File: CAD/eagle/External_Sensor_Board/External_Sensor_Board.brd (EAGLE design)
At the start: 50.8 x 33 mm, 12 parts, among them J1 SFW15R_FFC, U1 MAX31725MTA+, U2 HSCMNNN1.6BAAA3

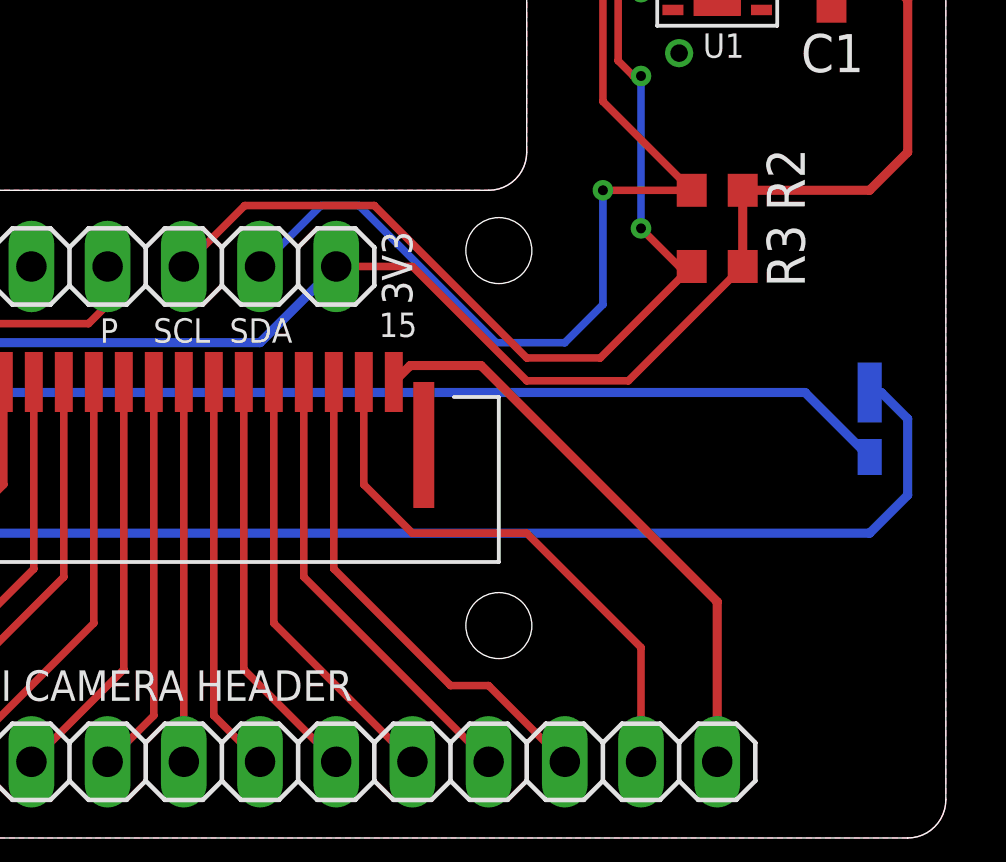
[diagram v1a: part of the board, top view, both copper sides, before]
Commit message: Added I2C buffer to external sensor board.
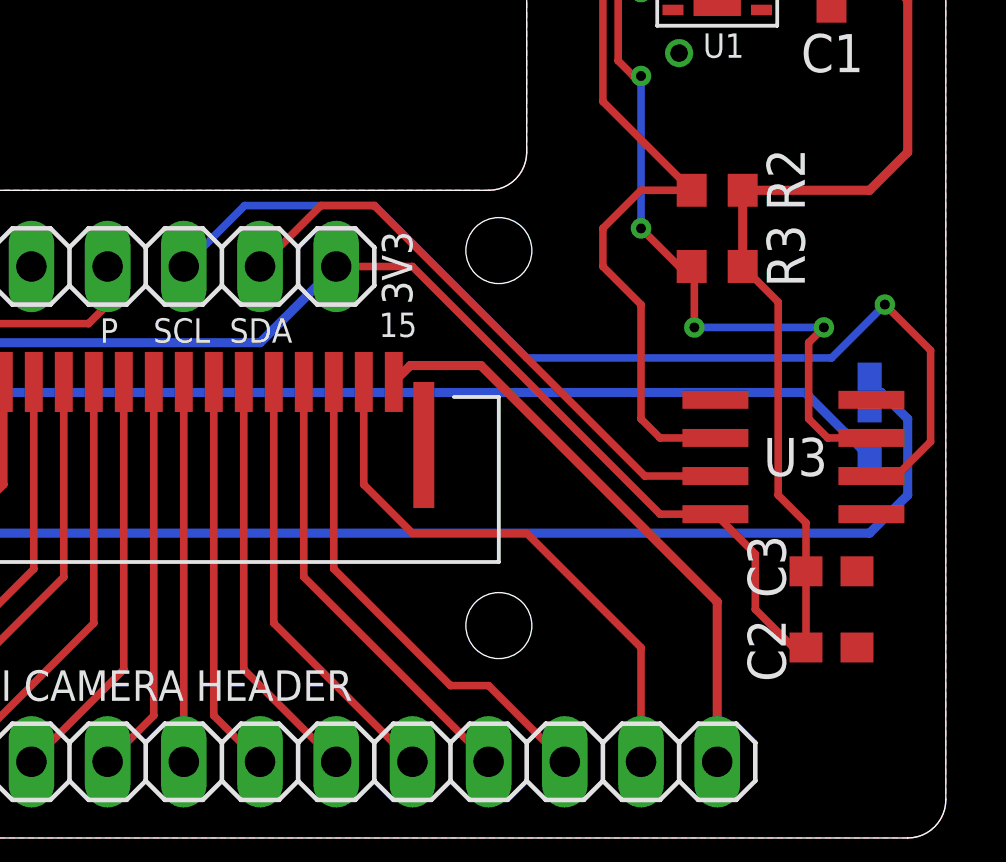
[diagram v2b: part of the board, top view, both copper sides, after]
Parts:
- added C2: 1uF, resistor:C0603
- added C3: 100nF, resistor:C0603
- added U3: P82B715, CM_IC:SO8
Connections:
- new net SCL_BUFF: JP1.3, U3.2
- new net SDA_BUFF: JP1.2, U3.7
- net +3V3: now also C2.1, C3.1, U3.8
- net GND: now also C2.2, C3.2, U3.4
- net SCL: now also U3.3; no longer JP1.3
- net SDA: now also U3.6; no longer JP1.2
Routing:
- net SCL_BUFF: track 0.00 -> 34.7 mm, vias 0 -> 1
- net SDA_BUFF: track 0.00 -> 19.8 mm
- net +3V3: track 71.2 -> 90.0 mm
- net SCL: track 34.0 -> 24.9 mm, vias 2 -> 4
- net SDA: track 32.8 -> 24.4 mm, vias 1 -> 0
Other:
- board text removed: "OPTIONAL"
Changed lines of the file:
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@@
 <layer number="48" name="Document" color="7" fill="1" visible="yes" active="yes"/>
 <layer number="49" name="Reference" color="7" fill="1" visible="yes" active="yes"/>
+<layer number="50" name="dxf" color="7" fill="1" visible="no" active="no"/>
 <layer number="51" name="tDocu" color="7" fill="1" visible="yes" active="yes"/>
 <layer number="52" name="bDocu" color="7" fill="1" visible="yes" active="yes"/>
@@
 <layer number="98" name="Guide" color="6" fill="1" visible="no" active="no"/>
 <layer number="99" name="SpiceOrder" color="5" fill="1" visible="no" active="no"/>
+<layer number="100" name="Muster" color="7" fill="1" visible="no" active="no"/>
+<layer number="101" name="Patch_Top" color="12" fill="4" visible="yes" active="yes"/>
+<layer number="116" name="Patch_BOT" color="9" fill="4" visible="yes" active="yes"/>
+<layer number="200" name="200bmp" color="1" fill="10" visible="no" active="no"/>
+<layer number="250" name="Descript" color="3" fill="1" visible="yes" active="yes"/>
+<layer number="251" name="SMDround" color="12" fill="11" visible="no" active="no"/>
 </layers>
 <board>
@@
 <text x="24.384" y="16.51" size="0.8128" layer="21">SCL</text>
 <text x="26.924" y="16.51" size="0.8128" layer="21">SDA</text>
-<text x="49.53" y="17.78" size="0.8128" layer="51" rot="R180">I2C PULLUPS</text>
-<text x="47.244" y="16.764" size="0.8128" layer="51" rot="R180">OPTIONAL</text>
+<text x="46.228" y="24.384" size="0.8128" layer="51" rot="R270">I2C PULLUPS</text>
 <dimension x1="0" y1="31.75" x2="50.8" y2="27.94" x3="25.4" y3="39.37" textsize="0.8128" layer="49" dtype="horizontal" unit="inch"/>
 <dimension x1="38.1" y1="31.75" x2="37.201975" y2="32.648025" x3="31.686540625" y3="38.163459375" textsize="0.8128" layer="49" dtype="radius" unit="inch"/>
@@
 <attribute name="NAME" x="2.794" y="21.844" size="0.8128" layer="25" rot="R180"/>
 </element>
+<element name="U3" library="CM_IC" package="SO8" value="P82B715" x="45.72" y="12.7" smashed="yes" rot="R90">
+<attribute name="NAME" x="46.863" y="13.335" size="1.27" layer="25" rot="R180"/>
+</element>
+<element name="C2" library="resistor" package="C0603" value="1uF" x="46.99" y="6.35" smashed="yes">
+<attribute name="NAME" x="45.466" y="5.207" size="1.27" layer="25" rot="R90"/>
+</element>
+<element name="C3" library="resistor" package="C0603" value="100nF" x="46.99" y="8.89" smashed="yes">
+<attribute name="NAME" x="45.466" y="8.001" size="1.27" layer="25" rot="R90"/>
+</element>
 </elements>
 <signals>
@@
 <wire x1="44.655" y1="30.685" x2="45.1925" y2="31.2225" width="0.3048" layer="1"/>
 <wire x1="30.48" y1="19.05" x2="33.02" y2="19.05" width="0.254" layer="1"/>
-<wire x1="33.02" y1="19.05" x2="36.83" y2="15.24" width="0.254" layer="1"/>
-<wire x1="36.83" y1="15.24" x2="40.22" y2="15.24" width="0.254" layer="1"/>
-<wire x1="40.22" y1="15.24" x2="44.03" y2="19.05" width="0.254" layer="1"/>
+<contactref element="C2" pad="1"/>
+<contactref element="C3" pad="1"/>
+<contactref element="U3" pad="8"/>
+<wire x1="33.02" y1="19.05" x2="41.275" y2="10.795" width="0.254" layer="1"/>
+<wire x1="41.275" y1="10.795" x2="43.12" y2="10.795" width="0.254" layer="1"/>
+<wire x1="45.212" y1="11.43" x2="45.212" y2="17.868" width="0.254" layer="1"/>
+<wire x1="45.212" y1="17.868" x2="44.03" y2="19.05" width="0.254" layer="1"/>
+<wire x1="45.212" y1="11.43" x2="46.14" y2="10.502" width="0.254" layer="1"/>
+<wire x1="46.14" y1="10.502" x2="46.14" y2="8.89" width="0.254" layer="1"/>
+<wire x1="46.14" y1="8.89" x2="46.14" y2="6.35" width="0.254" layer="1"/>
+<wire x1="43.12" y1="10.795" x2="44.45" y2="9.465" width="0.254" layer="1"/>
+<wire x1="44.45" y1="9.465" x2="44.45" y2="7.62" width="0.254" layer="1"/>
+<wire x1="44.45" y1="7.62" x2="45.72" y2="6.35" width="0.254" layer="1"/>
+<wire x1="45.72" y1="6.35" x2="46.14" y2="6.35" width="0.254" layer="1"/>
 </signal>
 <signal name="GND">
@@
 </polygon>
 <via x="41.91" y="26.162" extent="1-16" drill="0.5842"/>
+<contactref element="U3" pad="4"/>
+<contactref element="C3" pad="2"/>
+<contactref element="C2" pad="2"/>
 </signal>
 <signal name="SDA">
 <contactref element="U1" pad="1"/>
 <contactref element="R2" pad="2"/>
-<contactref element="JP1" pad="2"/>
-<via x="39.37" y="21.59" extent="1-16" drill="0.3302"/>
-<wire x1="39.37" y1="21.59" x2="42.33" y2="21.59" width="0.254" layer="1"/>
 <wire x1="42.33" y1="21.59" x2="39.37" y2="24.55" width="0.254" layer="1"/>
 <wire x1="39.37" y1="24.55" x2="39.37" y2="29.21" width="0.254" layer="1"/>
 <wire x1="39.37" y1="29.21" x2="39.71" y2="29.55" width="0.254" layer="1"/>
 <wire x1="39.71" y1="29.55" x2="41.705" y2="29.55" width="0.254" layer="1"/>
-<wire x1="27.94" y1="19.05" x2="29.972" y2="21.082" width="0.254" layer="16"/>
-<wire x1="29.972" y1="21.082" x2="31.242" y2="21.082" width="0.254" layer="16"/>
-<wire x1="31.242" y1="21.082" x2="35.814" y2="16.51" width="0.254" layer="16"/>
-<wire x1="35.814" y1="16.51" x2="38.1" y2="16.51" width="0.254" layer="16"/>
-<wire x1="38.1" y1="16.51" x2="39.37" y2="17.78" width="0.254" layer="16"/>
-<wire x1="39.37" y1="17.78" x2="39.37" y2="21.59" width="0.254" layer="16"/>
+<contactref element="U3" pad="6"/>
+<wire x1="43.12" y1="13.335" x2="41.275" y2="13.335" width="0.254" layer="1"/>
+<wire x1="41.275" y1="13.335" x2="40.64" y2="13.97" width="0.254" layer="1"/>
+<wire x1="40.64" y1="13.97" x2="40.64" y2="17.78" width="0.254" layer="1"/>
+<wire x1="40.64" y1="17.78" x2="39.37" y2="19.05" width="0.254" layer="1"/>
+<wire x1="39.37" y1="19.05" x2="39.37" y2="20.32" width="0.254" layer="1"/>
+<wire x1="39.37" y1="20.32" x2="40.64" y2="21.59" width="0.254" layer="1"/>
+<wire x1="40.64" y1="21.59" x2="42.33" y2="21.59" width="0.254" layer="1"/>
 </signal>
 <signal name="SCL">
 <contactref element="U1" pad="2"/>
 <contactref element="R3" pad="2"/>
-<contactref element="JP1" pad="3"/>
 <wire x1="42.33" y1="19.05" x2="41.91" y2="19.05" width="0.254" layer="1"/>
 <via x="40.64" y="20.32" extent="1-16" drill="0.3302"/>
@@
 <wire x1="41.649" y1="28.956" x2="41.705" y2="28.9" width="0.254" layer="1"/>
 <wire x1="40.64" y1="20.32" x2="41.91" y2="19.05" width="0.254" layer="1"/>
-<wire x1="25.4" y1="19.05" x2="27.432" y2="21.082" width="0.254" layer="1"/>
-<wire x1="27.432" y1="21.082" x2="31.75" y2="21.082" width="0.254" layer="1"/>
-<wire x1="31.75" y1="21.082" x2="36.83" y2="16.002" width="0.254" layer="1"/>
-<wire x1="36.83" y1="16.002" x2="39.282" y2="16.002" width="0.254" layer="1"/>
-<wire x1="39.282" y1="16.002" x2="42.33" y2="19.05" width="0.254" layer="1"/>
+<contactref element="U3" pad="3"/>
+<wire x1="48.32" y1="13.335" x2="46.863" y2="13.335" width="0.254" layer="1"/>
+<wire x1="46.863" y1="13.335" x2="46.228" y2="13.97" width="0.254" layer="1"/>
+<wire x1="46.228" y1="13.97" x2="46.228" y2="16.51" width="0.254" layer="1"/>
+<wire x1="46.228" y1="16.51" x2="46.736" y2="17.018" width="0.254" layer="1"/>
+<via x="46.736" y="17.018" extent="1-16" drill="0.3302"/>
+<wire x1="46.736" y1="17.018" x2="42.418" y2="17.018" width="0.254" layer="16"/>
+<via x="42.418" y="17.018" extent="1-16" drill="0.3302"/>
+<wire x1="42.418" y1="17.018" x2="42.418" y2="18.962" width="0.254" layer="1"/>
+<wire x1="42.418" y1="18.962" x2="42.33" y2="19.05" width="0.254" layer="1"/>
 </signal>
 <signal name="N$1">
@@
 <wire x1="27.4" y1="5.62" x2="27.4" y2="15.2" width="0.254" layer="1"/>
 </signal>
+<signal name="SDA_BUFF">
+<contactref element="U3" pad="7"/>
+<contactref element="JP1" pad="2"/>
+<wire x1="27.94" y1="19.05" x2="29.972" y2="21.082" width="0.254" layer="1"/>
+<wire x1="29.972" y1="21.082" x2="31.75" y2="21.082" width="0.254" layer="1"/>
+<wire x1="31.75" y1="21.082" x2="40.767" y2="12.065" width="0.254" layer="1"/>
+<wire x1="40.767" y1="12.065" x2="43.12" y2="12.065" width="0.254" layer="1"/>
+</signal>
+<signal name="SCL_BUFF">
+<contactref element="U3" pad="2"/>
+<contactref element="JP1" pad="3"/>
+<wire x1="25.4" y1="19.05" x2="27.432" y2="21.082" width="0.254" layer="16"/>
+<wire x1="27.432" y1="21.082" x2="31.75" y2="21.082" width="0.254" layer="16"/>
+<wire x1="31.75" y1="21.082" x2="36.83" y2="16.002" width="0.254" layer="16"/>
+<wire x1="36.83" y1="16.002" x2="46.99" y2="16.002" width="0.254" layer="16"/>
+<wire x1="46.99" y1="16.002" x2="48.768" y2="17.78" width="0.254" layer="16"/>
+<via x="48.768" y="17.78" extent="1-16" drill="0.3302"/>
+<wire x1="48.768" y1="17.78" x2="50.292" y2="16.256" width="0.254" layer="1"/>
+<wire x1="50.292" y1="16.256" x2="50.292" y2="13.208" width="0.254" layer="1"/>
+<wire x1="50.292" y1="13.208" x2="49.149" y2="12.065" width="0.254" layer="1"/>
+<wire x1="49.149" y1="12.065" x2="48.32" y2="12.065" width="0.254" layer="1"/>
+</signal>
 </signals>

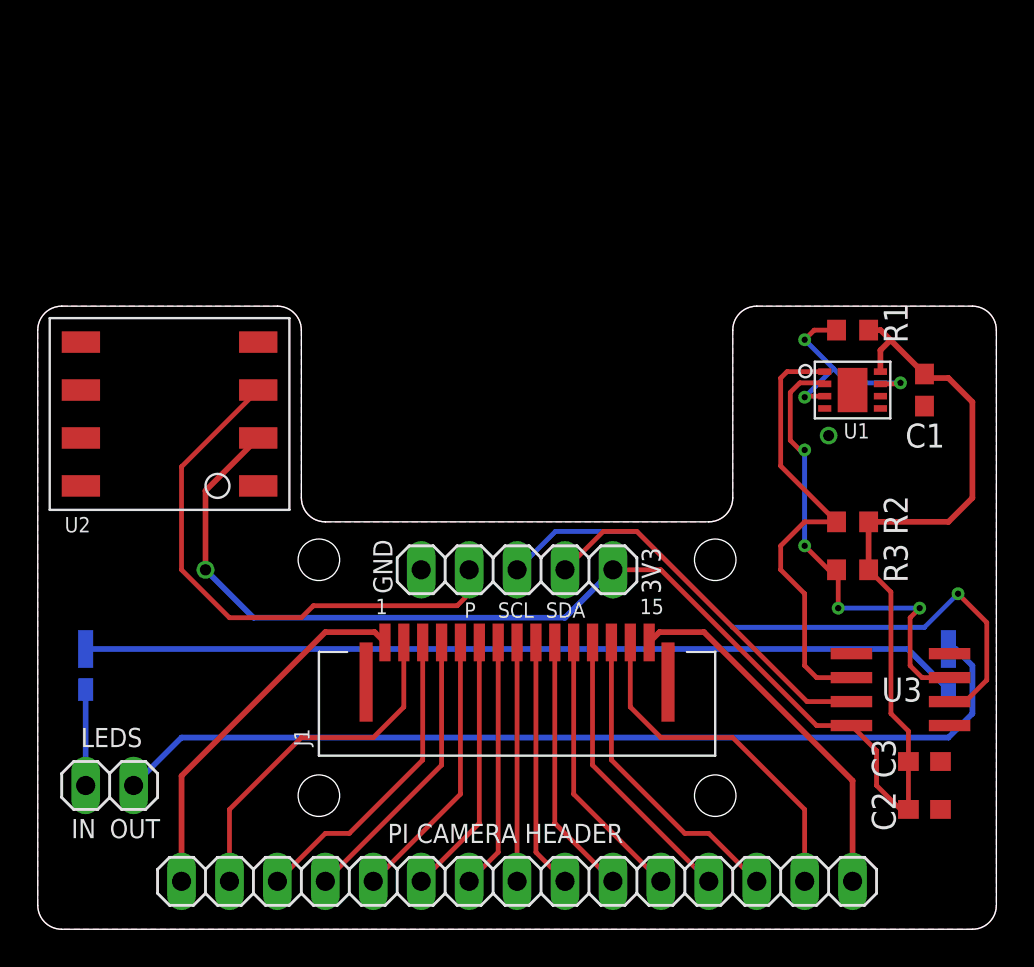
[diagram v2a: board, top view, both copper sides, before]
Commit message: Altered external sensor board to use J30J-25 connector instead of headers. Board is final aside from logos.
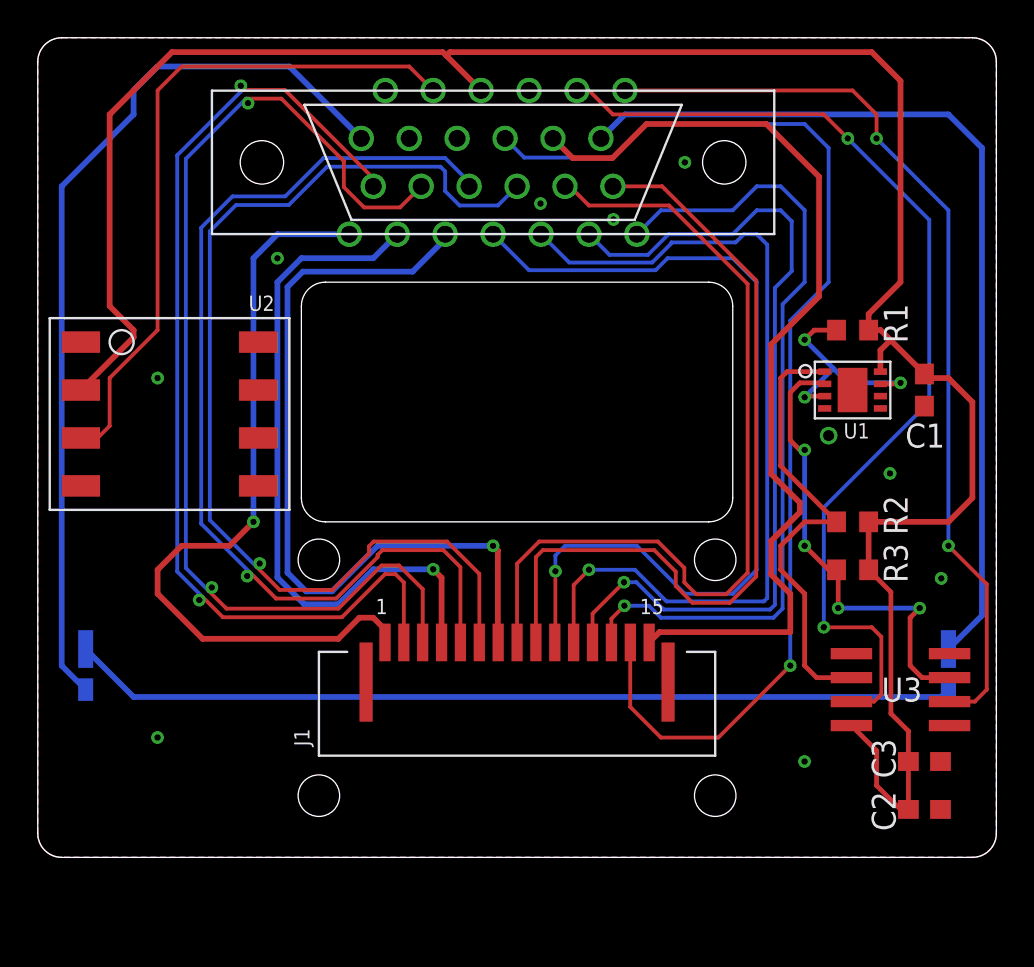
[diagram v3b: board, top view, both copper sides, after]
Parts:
- removed JP1: (no value), pinhead:1X05
- removed JP2: (no value), pinhead:1X15
- removed JP3: (no value), pinhead:1X02
- added J2: J30J-25, CM_J30J:ZKN-25
- turned U2 to 270 degrees
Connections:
- removed net CAM_CN: J1.8, JP2.8
- removed net CAM_CP: J1.9, JP2.9
- removed net CAM_DN0: J1.2, JP2.2
- removed net CAM_DN1: J1.5, JP2.5
- removed net CAM_DP0: J1.3, JP2.3
- removed net CAM_DP1: J1.6, JP2.6
- new net CAM_C_N: J1.8, J2.10
- new net CAM_C_P: J1.9, J2.12
- new net CAM_D0_N: J1.2, J2.2
- new net CAM_D0_P: J1.3, J2.4
- new net CAM_D1_N: J1.5, J2.6
- new net CAM_D1_P: J1.6, J2.8
- net +3V3: now also J2.19; no longer JP1.1
- net CAM_3V3: now also J2.22; no longer JP2.15
- net CAM_GND1: now also J2.1; no longer JP2.1
- net CAM_GND2: now also J2.3; no longer JP2.4
- net CAM_GND3: now also J2.5; no longer JP2.7
- net CAM_GND4: now also J2.7; no longer JP2.10
- net CAM_GPIO0: now also J2.9; no longer JP2.11
- net CAM_GPIO1: now also J2.11; no longer JP2.12
- net CAM_SCL: now also J2.13; no longer JP2.13
- net CAM_SDA: now also J2.20; no longer JP2.14
- net GND: now also J2.15; no longer JP1.5
- net LED_IN: now also J2.14; no longer JP3.1
- net LED_OUT: now also J2.24; no longer JP3.2
- net POUT: now also J2.17; no longer JP1.4
- net SCL_BUFF: now also J2.25; no longer JP1.3
- net SDA_BUFF: now also J2.23; no longer JP1.2
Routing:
- net CAM_D0_P: track 0.00 -> 57.9 mm, vias 0 -> 2
- net CAM_D1_P: track 0.00 -> 56.8 mm, vias 0 -> 1
- net CAM_D0_N: track 0.00 -> 54.5 mm, vias 0 -> 2
- net CAM_D1_N: track 0.00 -> 53.5 mm, vias 0 -> 1
- net CAM_C_N: track 0.00 -> 46.1 mm
- net CAM_C_P: track 0.00 -> 43.9 mm
- net LED_IN: track 5.08 -> 48.0 mm
- net CAM_SDA: track 18.7 -> 61.2 mm, vias 0 -> 1
- net CAM_GND4: track 14.0 -> 47.9 mm, vias 0 -> 1
- net SDA_BUFF: track 19.8 -> 53.5 mm, vias 0 -> 2
- net CAM_GPIO0: track 14.6 -> 46.6 mm, vias 0 -> 1
- net CAM_3V3: track 19.6 -> 51.0 mm
- net CAM_GPIO1: track 15.2 -> 45.7 mm, vias 0 -> 1
- net CAM_GND3: track 13.3 -> 42.3 mm, vias 0 -> 1
- net +3V3: track 90.0 -> 119.0 mm, vias 1 -> 0
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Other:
- board size 50.8 x 33 mm -> 50.8 x 43.4 mm
- board text added: "REV 1.1 Feb. 2017"
- board text removed: "3V3"
- board text removed: "GND"
- board text removed: "IN"
- board text removed: "LEDS"
- board text removed: "OUT"
- board text removed: "P"
- board text removed: "PI CAMERA HEADER"
- board text removed: "REV 1 Feb. 2017"
- board text removed: "SCL"
- board text removed: "SDA"
